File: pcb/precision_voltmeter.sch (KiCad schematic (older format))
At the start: 78 parts, among them J1 IN_PLUS, J10 shield clip, J11 shield clip, J12 shield clip, J13 shield clip, J14 IN_MINUS, J15 Conn_01x04, J16 Conn_01x03, J2 IN_MINUS, J3 IN_PLUS_LV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

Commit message: SCH ONLY, add bodge filter caps
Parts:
- added C?: 100n, Capacitor_SMD:C_0805_2012Metric_Pad1.18x1.45mm_HandSolder, symbol Device:C
- added C?: 220p, Capacitor_SMD:C_0805_2012Metric_Pad1.18x1.45mm_HandSolder, symbol Device:C
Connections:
- net GND: now also C?.2, C?.2
- net at C5.1, JP2.1, JP2.2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: now also C?.1
- net at R5.1, U3.3 (VIN): now also C?.1
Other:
- moved on the sheet: R5
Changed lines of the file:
@@
 L Device:R R5
 U 1 1 614C48F8
-P 5850 5000
-F 0 "R5" V 5643 5000 50  0000 C CNN
-F 1 "4.7k" V 5734 5000 50  0000 C CNN
-F 2 "Resistor_SMD:R_0805_2012Metric_Pad1.20x1.40mm_HandSolder" V 5780 5000 50  0001 C CNN
-F 3 "~" H 5850 5000 50  0001 C CNN
-	1    5850 5000
+P 5600 5000
+F 0 "R5" V 5393 5000 50  0000 C CNN
+F 1 "4.7k" V 5484 5000 50  0000 C CNN
+F 2 "Resistor_SMD:R_0805_2012Metric_Pad1.20x1.40mm_HandSolder" V 5530 5000 50  0001 C CNN
+F 3 "~" H 5600 5000 50  0001 C CNN
+	1    5600 5000
 	0    1    1    0
 $EndComp
@@
 	8850 3200 9350 3200
 Wire Wire Line
-	6200 5000 6000 5000
-Text Notes 5900 5100 0    50   ~ 0
+	6200 5000 5950 5000
+Text Notes 5800 4950 0    50   ~ 0
 keep short
 Connection ~ 3850 5100
@@
 	4150 5000 4150 5300
 Wire Wire Line
-	4150 5300 5950 5300
+	4150 5300 4950 5300
 Connection ~ 5950 5300
 Wire Wire Line
-	5700 5000 5400 5000
+	5450 5000 5400 5000
 Wire Wire Line
 	5400 5000 5400 4050
@@
 	3850 4600 6100 4600
 Wire Wire Line
-	4400 4700 6200 4700
+	4400 4700 4950 4700
 Wire Wire Line
 	4050 4450 4050 4700
@@
 Wire Wire Line
 	1250 5600 1700 5600
+$Comp
+L Device:C C?
+U 1 1 614E2E43
+P 4950 4950
+F 0 "C?" H 5065 4996 50  0000 L CNN
+F 1 "100n" H 5065 4905 50  0000 L CNN
+F 2 "Capacitor_SMD:C_0805_2012Metric_Pad1.18x1.45mm_HandSolder" H 4988 4800 50  0001 C CNN
+F 3 "~" H 4950 4950 50  0001 C CNN
+	1    4950 4950
+	1    0    0    -1
+$EndComp
+$Comp
+L Device:C C?
+U 1 1 614E3586
+P 5950 5150
+F 0 "C?" H 6065 5196 50  0000 L CNN
+F 1 "220p" H 6065 5105 50  0000 L CNN
+F 2 "Capacitor_SMD:C_0805_2012Metric_Pad1.18x1.45mm_HandSolder" H 5988 5000 50  0001 C CNN
+F 3 "~" H 5950 5150 50  0001 C CNN
+	1    5950 5150
+	1    0    0    -1
+$EndComp
+Connection ~ 5950 5000
+Wire Wire Line
+	5950 5000 5750 5000
+Wire Wire Line
+	4950 4800 4950 4700
+Connection ~ 4950 4700
+Wire Wire Line
+	4950 4700 6200 4700
+Wire Wire Line
+	4950 5100 4950 5300
+Connection ~ 4950 5300
+Wire Wire Line
+	4950 5300 5950 5300
+Text Notes 5650 4700 0    50   ~ 0
+keep short
 $EndSCHEMATC

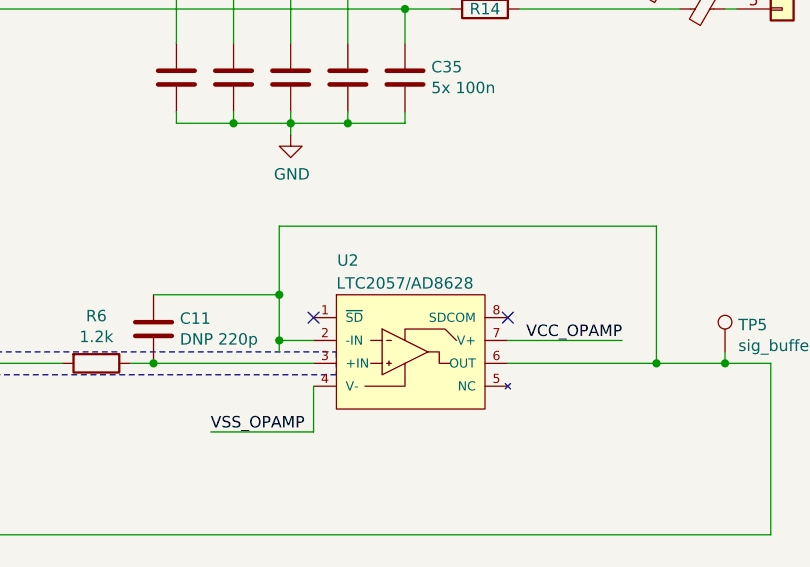
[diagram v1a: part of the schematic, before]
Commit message: Add power bodge board
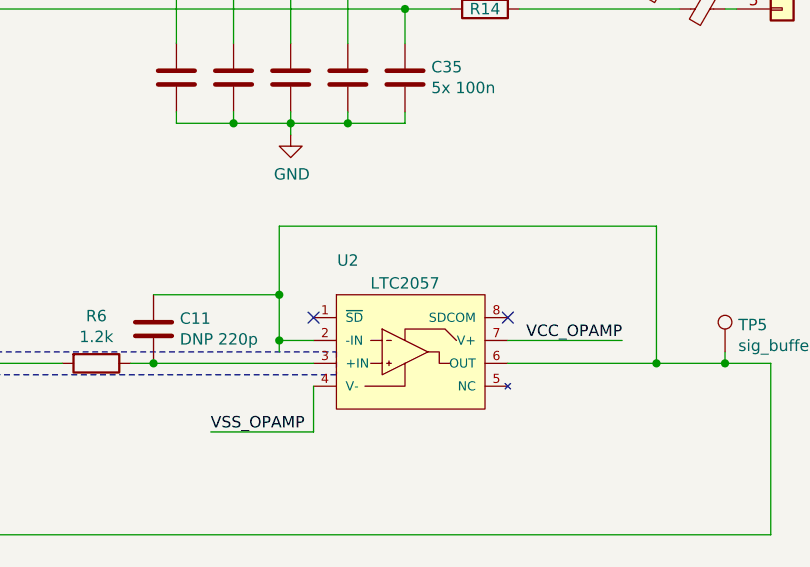
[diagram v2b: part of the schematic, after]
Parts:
- U2: value LTC2057/AD8628 -> LTC2057
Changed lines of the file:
@@
 P 8450 3250
 F 0 "U2" H 8150 3650 50  0000 C CNN
-F 1 "LTC2057/AD8628" H 8400 3550 50  0000 C CNN
+F 1 "LTC2057" H 8400 3550 50  0000 C CNN
 F 2 "Package_SO:SOIC-8_3.9x4.9mm_P1.27mm" H 8450 3250 50  0001 L BNN
 F 3 "" H 8450 3250 50  0001 L BNN
